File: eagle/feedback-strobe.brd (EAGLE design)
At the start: 39.9 x 17.7 mm, 17 parts, among them J2 MOTOR, U1 74LCX760SOIC20, U2 +12v, U3 V_REG_317SMD

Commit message: finished v1 PCB design
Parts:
- moved U3 43.4 mm to (34.2, 11.4), turned to 270 degrees
- moved C1 12.4 mm to (19.3, 8.64)
- moved U1 1.02 mm to (23.4, 10.4)
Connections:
- net GND: now also U1.P$1, U1.P$19
- net LED1: now also R4.2; no longer R1.2
- net LED2: now also R3.2; no longer R2.2
- net LED3: now also R2.2; no longer R3.2
- net LED4: now also R1.2; no longer R4.2
- net LED5: now also R8.2; no longer R5.2
- net LED6: now also R7.2; no longer R6.2
- net LED7: now also R6.2; no longer R7.2
- net LED8: now also R5.2; no longer R8.2
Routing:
- net 3V3: track 0.00 -> 44.4 mm, vias 0 -> 1
- net N$11: track 0.00 -> 37.6 mm, vias 0 -> 1
- net GND: track 0.00 -> 14.3 mm, vias 0 -> 6
- net LED_CTRL_1: track 0.00 -> 13.6 mm
- net LED4: track 0.00 -> 13.3 mm
- net LED5: track 0.00 -> 11.6 mm
- net LED_CTRL_2: track 0.00 -> 11.3 mm
- net LED6: track 0.00 -> 11.1 mm
- net N$9: track 0.00 -> 10.6 mm
- net LED3: track 0.00 -> 10.6 mm
- net LED7: track 0.00 -> 10.5 mm
- net LED8: track 0.00 -> 10.1 mm
- net LED_CTRL_5: track 0.00 -> 9.10 mm
- net LED_CTRL_3: track 0.00 -> 9.07 mm
- net LED2: track 0.00 -> 8.59 mm
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- added copper zone on layer 16, net GND

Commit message: edited mosfet label
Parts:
- U3: value V_REG_317SMD -> P CHAN MOSFET
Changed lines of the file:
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@@
 <attribute name="PROD_ID" value="VREG-12370" x="6.858" y="7.62" size="1.778" layer="28" rot="MR0" display="off"/>
 </element>
-<element name="U3" library="SparkFun-PowerIC" package="SOT223" value="V_REG_317SMD" x="34.163" y="11.43" rot="R270"/>
+<element name="U3" library="SparkFun-PowerIC" package="SOT223" value="P CHAN MOSFET" x="34.163" y="11.43" rot="R270"/>
 <element name="TEENSY" library="SparkFun-Connectors" package="1X13" value="" x="3.302" y="16.256"/>
 <element name="IR" library="SparkFun-Connectors" package="1X02" value="" x="36.322" y="1.524" rot="R180"/>

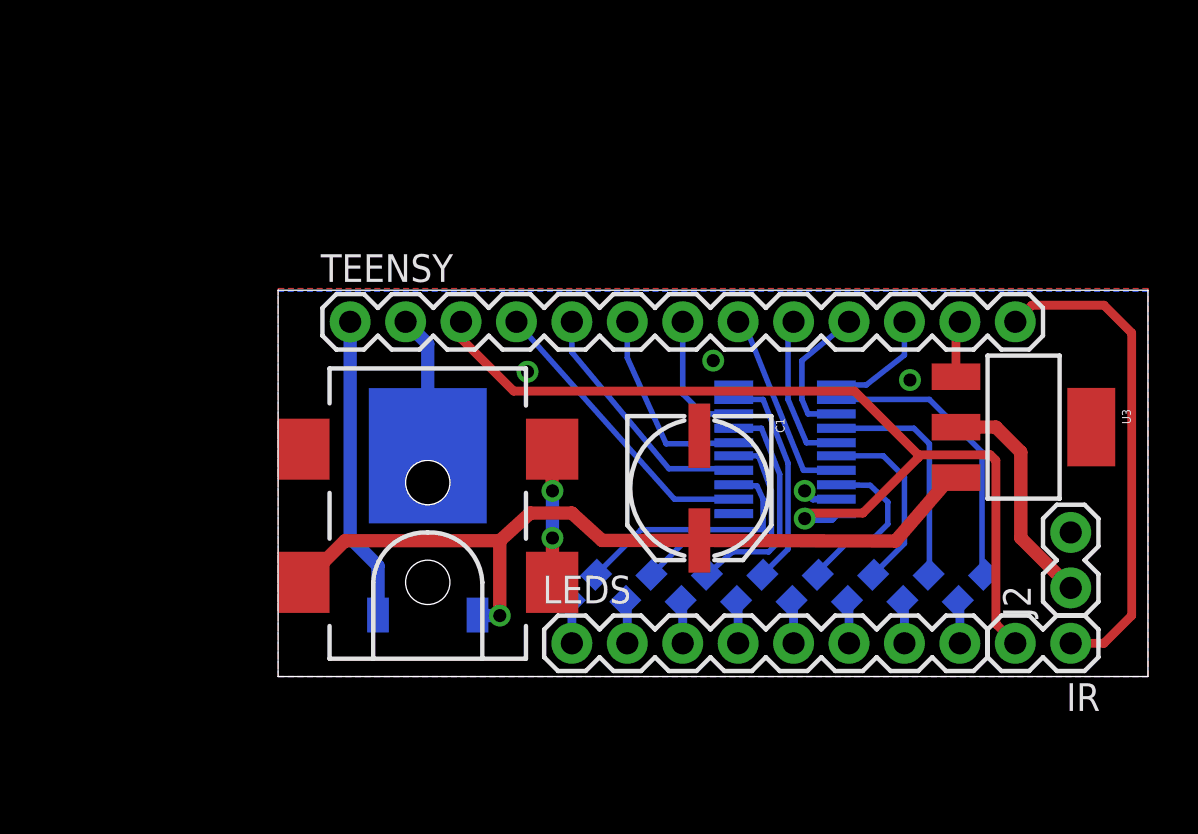
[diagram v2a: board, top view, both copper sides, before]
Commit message: new components added, new board dimensions set. routing started. mosfet footprint from digikey not wanting to connect nets
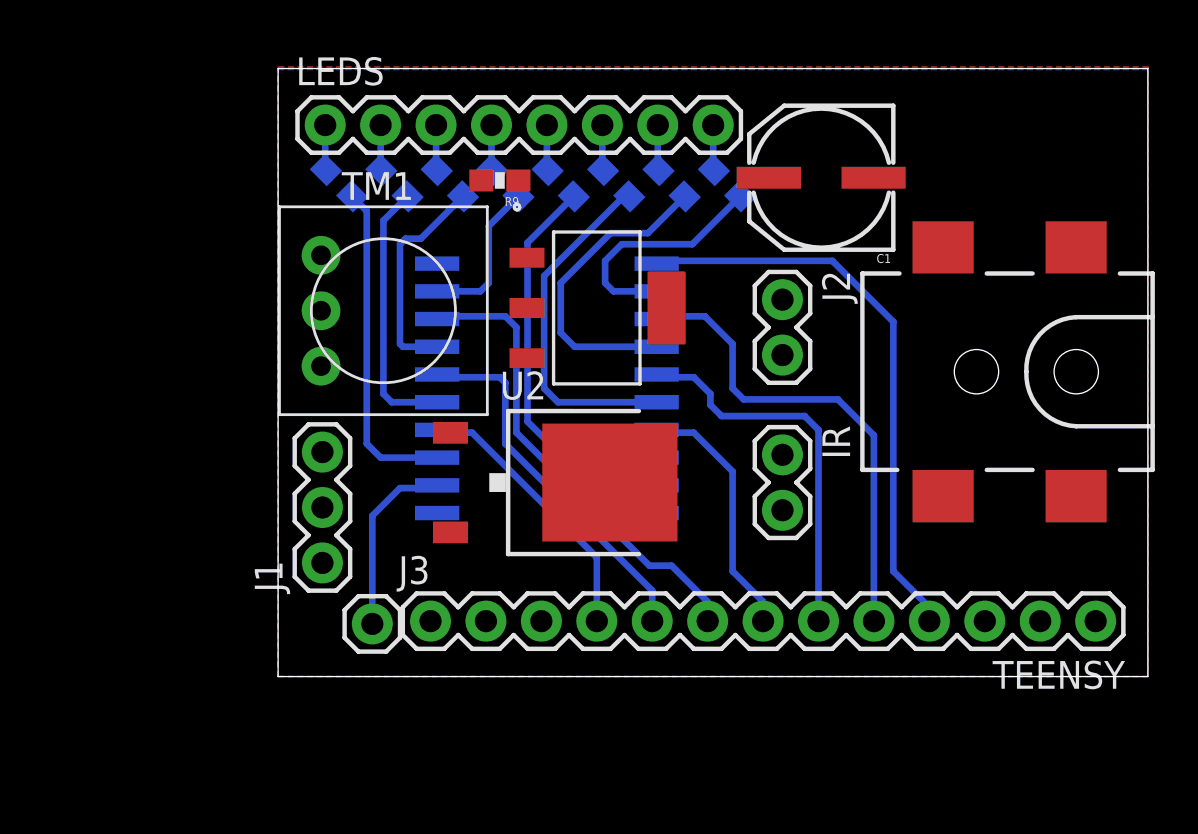
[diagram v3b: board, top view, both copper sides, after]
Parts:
- removed U3: P CHAN MOSFET, SparkFun-PowerIC:SOT223
- added J1: (no value), SparkFun-Connectors:1X03
- added J3: (no value), SparkFun-Connectors:1X01
- added LED_DRIVER: 74C923M, 74xx-us:SO20W
- added R9: (no value), SparkFun-Passives:0603-RES
- added TM1: (no value), adafruit:TRIM-3386
- U1: value 74LCX760SOIC20 -> STN3NF06L; device SparkFun-DigitalIC:SOIC-20 -> n-fet:SOT-223
- moved TEENSY 36.8 mm to (37.5, 2.54), turned to 180 degrees
- moved DC_IN 31.2 mm to (36.6, 14.0), turned to 180 degrees
- moved LEDS 26.3 mm to (2.16, 25.3)
- moved R2 21.6 mm to (18.0, 22.6), turned to 225 degrees
- moved R3 21.6 mm to (15.5, 22.6), turned to 225 degrees
- moved R6 21.6 mm to (7.87, 22.6), turned to 225 degrees
- moved R7 21.6 mm to (5.33, 22.6), turned to 225 degrees
- moved R1 21.6 mm to (20.6, 22.6), turned to 225 degrees
- moved R4 21.6 mm to (13.0, 22.6), turned to 225 degrees
- moved R5 21.6 mm to (10.4, 22.6), turned to 225 degrees
- moved R8 21.6 mm to (2.79, 22.6), turned to 225 degrees
- moved J2 18.7 mm to (23.1, 17.3), turned to 270 degrees
- moved IR 15.8 mm to (23.1, 10.2), turned to 270 degrees
- moved C1 15.3 mm to (24.9, 22.9), turned to 180 degrees
- moved U1 10.9 mm to (14.6, 16.9), flipped to the top, turned to 270 degrees
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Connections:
- removed net N$11: C1.+, DC_IN.VIN0, U2.1, U3.3
- removed net N$9: J2.1, U3.2
- new net BLINK_CTRL: TEENSY.12, TM1.2
- new net MOTOR_IN: J1.2, TEENSY.13
- new net N$8: J2.2
- new net VCC: LED_DRIVER.20
- new net VIN: C1.+, DC_IN.VIN0, J2.1, U2.1
- net 3V3: now also TM1.3; no longer U1.P$20
- net GND: now also J1.3, LED_DRIVER.1, LED_DRIVER.10, LED_DRIVER.19, R9.1, TM1.1; no longer J2.2, U1.P$1, U1.P$10, U1.P$19
- net IR_IN: now also J1.1; no longer TEENSY.13
- net LED1: now also LED_DRIVER.18; no longer U1.P$18
- net LED2: now also LED_DRIVER.16; no longer U1.P$16
- net LED3: now also LED_DRIVER.14; no longer U1.P$14
- net LED4: now also LED_DRIVER.12; no longer U1.P$12
- net LED5: now also LED_DRIVER.3; no longer U1.P$3
- net LED6: now also LED_DRIVER.5; no longer U1.P$5
- net LED7: now also LED_DRIVER.7; no longer U1.P$7
- net LED8: now also LED_DRIVER.9; no longer U1.P$9
- net LED_CTRL_1: now also J3.1, LED_DRIVER.2; no longer TEENSY.4, U1.P$2
- net LED_CTRL_2: now also LED_DRIVER.4, TEENSY.10; no longer TEENSY.5, U1.P$4
- net LED_CTRL_3: now also LED_DRIVER.6, TEENSY.9; no longer TEENSY.6, U1.P$6
- net LED_CTRL_4: now also LED_DRIVER.8, TEENSY.8; no longer TEENSY.7, U1.P$8
- net LED_CTRL_5: now also LED_DRIVER.17, TEENSY.7; no longer TEENSY.8, U1.P$17
- net LED_CTRL_6: now also LED_DRIVER.15, TEENSY.6; no longer TEENSY.9, U1.P$15
- net LED_CTRL_7: now also LED_DRIVER.13, TEENSY.5; no longer TEENSY.10, U1.P$13
- net LED_CTRL_8: now also LED_DRIVER.11, TEENSY.4; no longer TEENSY.11, U1.P$11
- net MOTOR_CTRL: now also R9.2, U1.1; no longer TEENSY.12, U3.1
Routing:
- net 3V3: track 44.4 -> 0.00 mm, vias 1 -> 0
- net N$11: track 37.6 -> 0.00 mm, vias 1 -> 0
- net IR_IN: track 22.4 -> 0.00 mm
- net LED_CTRL_8: track 5.12 -> 26.5 mm
- net LED_CTRL_4: track 6.02 -> 21.6 mm
- net LED_CTRL_7: track 6.59 -> 22.0 mm
- net GND: track 14.3 -> 0.00 mm, vias 6 -> 0
- net 5V: track 14.0 -> 0.00 mm
- net N$9: track 10.6 -> 0.00 mm
- net LED_CTRL_6: track 7.19 -> 17.5 mm
- net LED1: track 7.92 -> 17.8 mm
- net LED_CTRL_3: track 9.07 -> 17.0 mm
- net LED2: track 8.59 -> 16.0 mm
- net LED_CTRL_1: track 13.6 -> 8.50 mm
- net LED3: track 10.6 -> 14.3 mm
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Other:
- board size 39.9 x 17.7 mm -> 39.9 x 27.9 mm

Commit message: initial completion of v2 pcb design
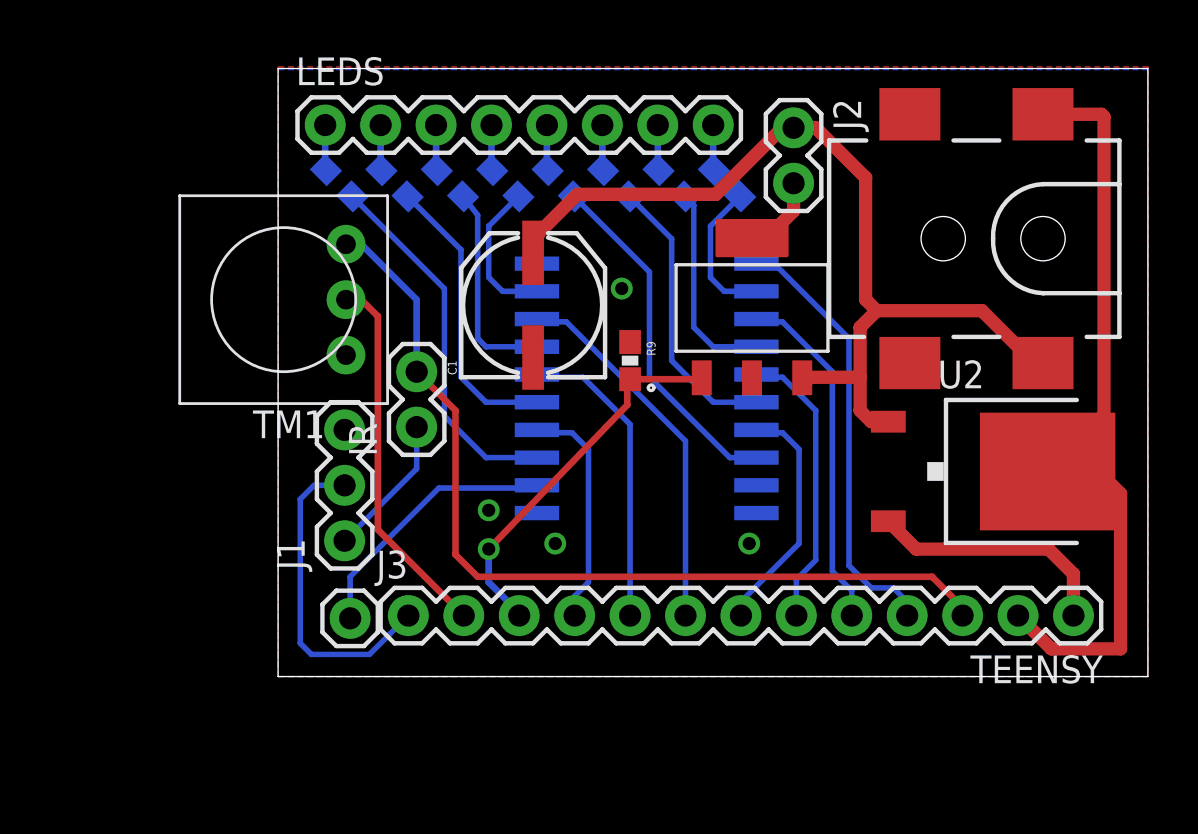
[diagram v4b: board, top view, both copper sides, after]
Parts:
- moved U2 20.1 mm to (32.8, 9.40)
- moved IR 16.8 mm to (6.35, 11.4), turned to 90 degrees
- moved C1 14.4 mm to (11.7, 17.0), turned to 90 degrees
- moved R9 10.2 mm to (16.1, 14.5), turned to 270 degrees
- moved J2 7.89 mm to (23.6, 25.1)
- moved U1 7.11 mm to (21.7, 16.9), turned to 0 degrees
- moved DC_IN 6.28 mm to (35.1, 20.1)
- moved TM1 4.60 mm to (0.25, 17.3), turned to 90 degrees
- moved LED_DRIVER 4.57 mm to (16.9, 13.2)
- moved J1 1.44 mm to (3.05, 6.22)
- moved TEENSY 1.05 mm to (36.4, 2.79)
- moved J3 1.05 mm to (3.30, 2.67)
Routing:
- net VIN: track 0.00 -> 43.4 mm
- net 3V3: track 0.00 -> 41.3 mm
- net GND: track 0.00 -> 36.4 mm, vias 0 -> 4
- net BLINK_CTRL: track 0.00 -> 17.1 mm
- net MOTOR_IN: track 0.00 -> 14.8 mm
- net N$4: track 0.00 -> 13.9 mm, vias 0 -> 1
- net 5V: track 0.00 -> 11.4 mm
- net IR_IN: track 0.00 -> 6.57 mm
- net LED_CTRL_8: track 26.5 -> 20.1 mm
- net LED_CTRL_7: track 22.0 -> 16.0 mm
- net LED3: track 14.3 -> 9.41 mm
- net LED_CTRL_4: track 21.6 -> 17.1 mm
- net LED_CTRL_6: track 17.5 -> 13.2 mm
- net LED4: track 10.9 -> 6.65 mm
- net LED_CTRL_1: track 8.50 -> 12.2 mm
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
